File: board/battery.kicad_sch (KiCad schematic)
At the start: 6 parts, among them J801 BAT

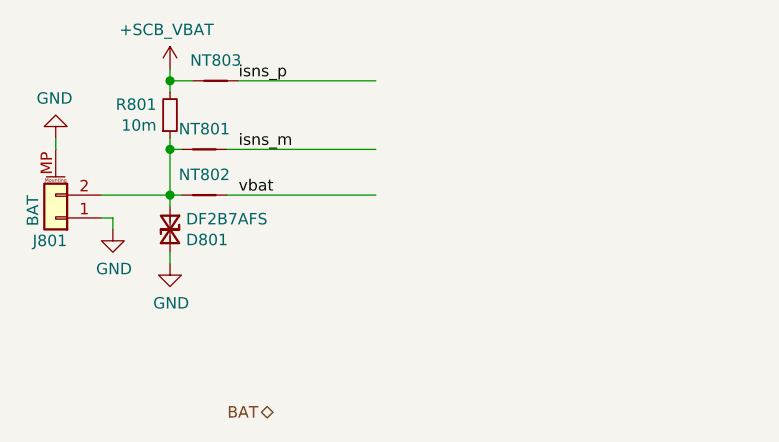
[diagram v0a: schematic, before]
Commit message: Added testpoints and other fixes
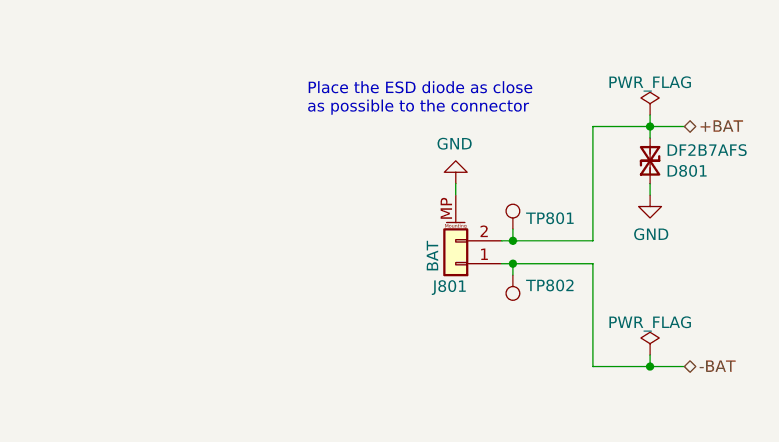
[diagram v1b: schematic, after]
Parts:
- removed NT801, NT802, NT803: Net-Tie_2, symbol Device:Net-Tie_2
- removed R801: 10m, symbol Device:R_Small
- added TP801, TP802: TestPoint, DIYPie:TestPoint_Pad_D1.5mm, symbol DIYPie:TestPoint
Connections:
- net GND: no longer J801.1 (Pin_1)
- net +BAT: now reaches D801.1 (A), J801.2 (Pin_2)
- net +BAT: now also TP801.1
- new net -BAT: J801.1 (Pin_1), TP802.1
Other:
- note added: "Place the ESD diode as close as possible to the connector"
- moved on the sheet: D801, J801
